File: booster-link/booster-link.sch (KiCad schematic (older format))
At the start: 20 parts, among them P1 Conn_01x04, P2 IBT-2, P3 EXTCON, P4 CONN_01X03, Q1 BC517, Q2 BC517, U1 7805, U2 6N137

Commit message: add ENABLE trigger
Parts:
- added C?: 1uF, symbol CP
- added C?: 100nF, w_capacitors:cnp_3mm_disc, symbol C
- added D?: 1N4148, w_pth_diodes:diode_do35, symbol D-RESCUE-booster-link
- added D?: LED_Small, symbol LED_Small
- added R?: 100k, w_pth_resistors:RC03, symbol R
- added R?: 47k, w_pth_resistors:RC03, symbol R
- added R?: 1k5, w_pth_resistors:RC03, symbol R
- added U?: TLC555CP, w_pth_circuits:dil_8-300_socket, symbol TLC555CP
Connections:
- net labels added: SIGNAL, t = 1,1 × R × C
- wire segments 71 -> 119
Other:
- moved on the sheet: C3, D1, D2, P1, P2, P3, P4, Q1, Q2, R1, R2, R3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

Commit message: wip
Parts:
- removed C?: 1uF, symbol CP
- removed D?: LED_Small, symbol LED_Small
- added C12: 2.2uF, Capacitors_ThroughHole:C_Rect_L7_W2_P5, symbol C
- added D3: Led_Small, LEDs:LED-5MM, symbol Led_Small
- R12: renamed from R?; value 47k -> 100k
- U2: symbol 6N136 -> 6N136-RESCUE-booster-link
- gave numbers to parts that had none: 5
- renumbered Q2 to Q21, R5 to R21, R6 to R22
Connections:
- net labels removed: t = 1,1 × R × C
- wire segments 119 -> 95
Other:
- note added: "t = 1,1 × R12 × C12\n t = 1,1 x 100.000 Ohm * 2,2 * 10e-6 F\n t = 232 ms"
- moved on the sheet: C11, D2, R7

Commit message: wip
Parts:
- D2, D3: footprint LEDs:LED-5MM -> LEDs:LED_D5.0mm
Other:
- moved on the sheet: C1, C11, C12, C2, C3, D1, D11, D2, D3, P1, P2, P3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

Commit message: add Gerber files
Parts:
- D2, D3: footprint LEDs:LED_D5.0mm -> LEDs:LED-5MM
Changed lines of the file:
@@
 LIBS:valves
 LIBS:microchip_pic16mcu
-LIBS:leds
 LIBS:booster-link-cache
 EELAYER 25 0
@@
 U 1 1 5B56C237
 P 3975 5850
-F 0 "U11" H 4225 6300 50  0000 L CNN
-F 1 "TLC555CP" H 4075 6200 50  0000 L CNN
+F 0 "U11" H 3900 5900 50  0000 L CNN
+F 1 "TLC555CP" H 3800 5775 50  0000 L CNN
 F 2 "w_pth_circuits:dil_8-300_socket" H 3975 5850 50  0001 C CNN
 F 3 "" H 3975 5850 50  0001 C CNN
@@
 F 0 "D2" H 5100 2200 50  0000 L CNN
 F 1 "Led_Small" H 4975 1975 50  0001 L CNN
-F 2 "LEDs:LED_D5.0mm" V 5150 2075 50  0001 C CNN
+F 2 "LEDs:LED-5MM" V 5150 2075 50  0001 C CNN
 F 3 "" V 5150 2075 50  0000 C CNN
 	1    5150 2075
@@
 F 0 "D3" H 7750 3950 50  0000 L CNN
 F 1 "Led_Small" H 7625 3725 50  0001 L CNN
-F 2 "LEDs:LED_D5.0mm" V 7800 3825 50  0001 C CNN
+F 2 "LEDs:LED-5MM" V 7800 3825 50  0001 C CNN
 F 3 "" V 7800 3825 50  0000 C CNN
 	1    7800 3825
 	0    -1   -1   0
 $EndComp
-Text Notes 5325 5325 0    60   ~ 0
+Text Notes 4750 5425 0    60   ~ 0
  t = 1,1 × R12 × C12\n t = 1,1 x 100.000 Ohm * 2,2 * 10e-6 F\n t = 232 ms
 $Comp

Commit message: wip
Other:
- moved on the sheet: C1, C11, C12, C2, C3, D1, D11, D2, D3, P1, P2, P3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

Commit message: wip
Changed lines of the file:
@@
 $EndComp
 Wire Wire Line
-	4500 1625 4550 1625
+	4500 1625 4900 1625
 Wire Wire Line
-	4550 1625 4900 1625
+	4100 1925 4100 2325
 Wire Wire Line
-	4100 1925 4100 2100
-Wire Wire Line
-	4100 2100 4100 2325
-Wire Wire Line
-	3450 2100 3650 2100
-Wire Wire Line
-	3650 2100 4100 2100
-Wire Wire Line
-	4100 2100 4550 2100
-Wire Wire Line
-	4550 2100 4900 2100
+	3450 2100 4900 2100
 Wire Wire Line
 	4550 2100 4550 2000
@@
 Connection ~ 4100 2100
 Wire Wire Line
-	3125 1625 3650 1625
-Wire Wire Line
-	3650 1625 3700 1625
+	3125 1625 3700 1625
 Wire Wire Line
 	3650 1625 3650 1750
@@
 Wire Wire Line
 	4900 1625 4900 1500
-Wire Wire Line
-	4900 2100 4900 2100
 Connection ~ 4550 2100
 Wire Wire Line
 	7050 3625 7150 3625
 Wire Wire Line
-	7050 3225 7750 3225
-Wire Wire Line
-	7750 3225 8150 3225
+	7050 3225 8150 3225
 Wire Wire Line
 	7750 3225 7750 3625
@@
 	4550 3525 4550 3575
 Wire Wire Line
-	4200 3525 4350 3525
-Wire Wire Line
-	4350 3525 4550 3525
+	4200 3525 4550 3525
 Connection ~ 4350 3525
 Wire Wire Line
-	3550 3825 4350 3825
-Wire Wire Line
-	4350 3825 4550 3825
+	3550 3825 4550 3825
 Wire Wire Line
 	4550 3825 4550 3775
@@
 	5250 3875 5250 4025
 Wire Wire Line
-	5150 2925 5150 3275
-Wire Wire Line
-	5150 3275 5150 3475
-Wire Wire Line
-	5150 3475 5150 3575
+	5150 2925 5150 3575
 Connection ~ 5150 3275
 Connection ~ 5150 3475
 Wire Wire Line
-	5150 3775 5325 3775
-Wire Wire Line
-	5325 3775 5750 3775
-Wire Wire Line
-	5750 3775 5800 3775
+	5150 3775 5800 3775
 Wire Wire Line
 	5325 3775 5325 3675
@@
 	6450 2925 6450 2975
 Wire Wire Line
-	6450 3275 6450 3525
-Wire Wire Line
-	6450 3525 6450 3575
+	6450 3275 6450 3575
 Wire Wire Line
 	5750 3325 7650 3325
@@
 	6850 1775 7250 1775
 Wire Wire Line
-	8150 1575 8150 1625
-Wire Wire Line
-	8150 1625 8150 1675
+	8150 1575 8150 1675
 Wire Wire Line
 	8150 2075 8150 2125
@@
 	7850 1875 7800 1875
 Wire Wire Line
-	6850 1875 7200 1875
-Wire Wire Line
-	7200 1875 7500 1875
+	6850 1875 7500 1875
 Wire Wire Line
 	5500 2175 5500 2275
 Wire Wire Line
-	4300 4600 4300 4725
-Wire Wire Line
-	4300 4725 4300 5075
+	4300 4600 4300 5075
 Wire Wire Line
 	4300 5875 4300 5975
 Wire Wire Line
-	4800 5475 4900 5475
+	4800 5475 5200 5475
 Wire Wire Line
-	4900 5475 5200 5475
-Wire Wire Line
-	4900 4725 4900 4975
-Wire Wire Line
-	4900 4975 4900 5475
-Wire Wire Line
-	4900 5475 4900 5675
+	4900 4725 4900 5675
 Wire Wire Line
 	4900 5675 4800 5675
@@
 	3800 4975 3700 4975
 Wire Wire Line
-	3700 4725 3700 4975
+	3700 4725 3700 5275
 Wire Wire Line
-	3700 4975 3700 5275
+	3200 5275 3800 5275
 Wire Wire Line
-	3200 5275 3700 5275
-Wire Wire Line
-	3700 5275 3800 5275
-Wire Wire Line
-	4100 4725 4300 4725
-Wire Wire Line
-	4300 4725 4500 4725
+	4100 4725 4500 4725
 Connection ~ 4300 4725
 Wire Wire Line

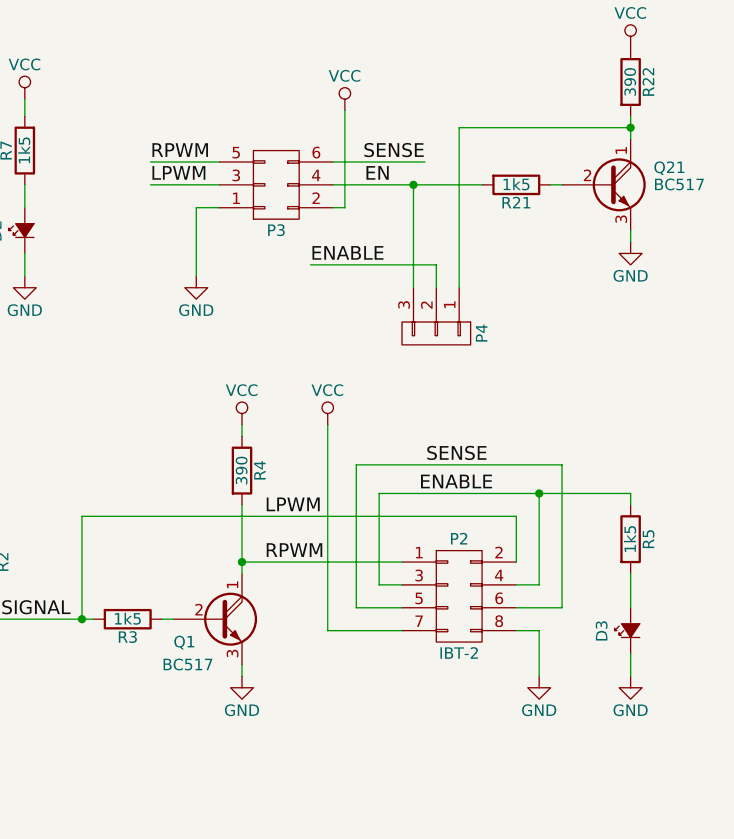
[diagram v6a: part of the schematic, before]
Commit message: BC517 -> BC337 taht works / add pictures
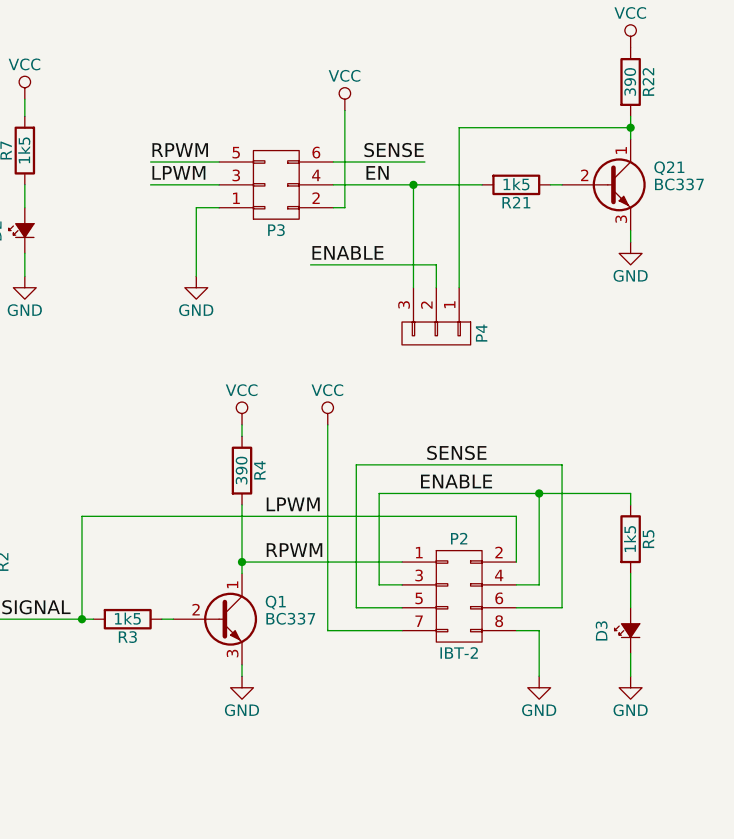
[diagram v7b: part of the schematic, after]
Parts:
- removed Q1, Q21: BC517, TO_SOT_Packages_THT:TO-92_Inline_Narrow_Oval, symbol BC517
- added Q1, Q21: BC337, TO_SOT_Packages_THT:TO-92_Molded_Narrow, symbol BC337
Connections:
- net GND: now also Q1.3 (E), Q21.3 (E)
- net RPWM: now also Q1.1 (C)
- net at R3.1: now also Q1.2 (B)
- net at P4.1 (P1), R22.2: now also Q21.1 (C)
- net at R21.1: now also Q21.2 (B)
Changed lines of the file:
@@
 SENSE
-$Comp
-L BC517 Q1
-U 1 1 5B55FBD7
-P 6350 3775
-F 0 "Q1" H 6150 3675 50  0000 L CNN
-F 1 "BC517" H 6100 3575 50  0000 L CNN
-F 2 "TO_SOT_Packages_THT:TO-92_Inline_Narrow_Oval" H 6550 3700 50  0001 L CIN
-F 3 "" H 6350 3775 50  0000 L CNN
-	1    6350 3775
-	1    0    0    -1
-$EndComp
-$Comp
-L BC517 Q21
-U 1 1 5B55FFFA
-P 8050 1875
-F 0 "Q21" H 8250 1950 50  0000 L CNN
-F 1 "BC517" H 8250 1875 50  0000 L CNN
-F 2 "TO_SOT_Packages_THT:TO-92_Inline_Narrow_Oval" H 8250 1800 50  0001 L CIN
-F 3 "" H 8050 1875 50  0000 L CNN
-	1    8050 1875
-	1    0    0    -1
-$EndComp
 $Comp
 L TLC555CP U11
@@
 	1    0    0    -1
 $EndComp
+$Comp
+L BC337 Q1
+U 1 1 5B6B104A
+P 6350 3775
+F 0 "Q1" H 6550 3850 50  0000 L CNN
+F 1 "BC337" H 6550 3775 50  0000 L CNN
+F 2 "TO_SOT_Packages_THT:TO-92_Molded_Narrow" H 6550 3700 50  0001 L CIN
+F 3 "" H 6350 3775 50  0001 L CNN
+	1    6350 3775
+	1    0    0    -1
+$EndComp
+$Comp
+L BC337 Q21
+U 1 1 5B6B12EF
+P 8050 1875
+F 0 "Q21" H 8250 1950 50  0000 L CNN
+F 1 "BC337" H 8250 1875 50  0000 L CNN
+F 2 "TO_SOT_Packages_THT:TO-92_Molded_Narrow" H 8250 1800 50  0001 L CIN
+F 3 "" H 8050 1875 50  0001 L CNN
+	1    8050 1875
+	1    0    0    -1
+$EndComp

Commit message: add some place for cap
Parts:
- Q1, Q21: footprint TO_SOT_Packages_THT:TO-92_Molded_Narrow -> TO_SOT_Packages_THT:TO-92_Inline_Narrow_Oval
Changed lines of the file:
@@
 Sheet 1 1
 Title "IBT-2 Booster"
-Date "2018-07-24"
+Date "2018-08-08"
 Rev "0.1"
 Comp "GBe"
@@
 F 0 "Q1" H 6550 3850 50  0000 L CNN
 F 1 "BC337" H 6550 3775 50  0000 L CNN
-F 2 "TO_SOT_Packages_THT:TO-92_Molded_Narrow" H 6550 3700 50  0001 L CIN
+F 2 "TO_SOT_Packages_THT:TO-92_Inline_Narrow_Oval" H 6550 3700 50  0001 L CIN
 F 3 "" H 6350 3775 50  0001 L CNN
 	1    6350 3775
@@
 F 0 "Q21" H 8250 1950 50  0000 L CNN
 F 1 "BC337" H 8250 1875 50  0000 L CNN
-F 2 "TO_SOT_Packages_THT:TO-92_Molded_Narrow" H 8250 1800 50  0001 L CIN
+F 2 "TO_SOT_Packages_THT:TO-92_Inline_Narrow_Oval" H 8250 1800 50  0001 L CIN
 F 3 "" H 8050 1875 50  0001 L CNN
 	1    8050 1875
